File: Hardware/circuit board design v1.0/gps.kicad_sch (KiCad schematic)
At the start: 1 part

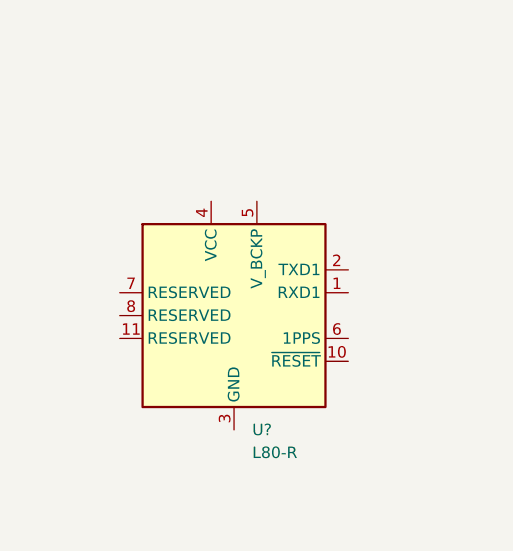
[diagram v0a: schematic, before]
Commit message: BMI088 schematic
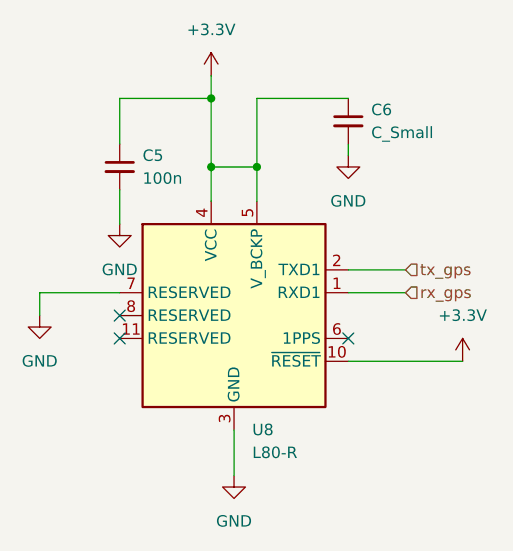
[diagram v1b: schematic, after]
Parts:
- added C5: 100n, symbol Device:C_Small
- added C6: C_Small, symbol Device:C_Small
- gave numbers to parts that had none: 1
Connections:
- net rx_gps: now reaches U8.1 (RXD1)
- net +3.3V: now reaches U8.10 (~{RESET})
- net +3.3V: now also U8.4 (VCC), U8.5 (V_BCKP), C5.1, C6.1
- net GND: now reaches U8.12 (GND), U8.3 (GND)
- net GND: now also U8.7 (RESERVED), C5.2, C6.2
- net tx_gps: now reaches U8.2 (TXD1)
- no-connect marks 0 -> 3
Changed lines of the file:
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@@
 (kicad_sch (version 20211123) (generator eeschema)
   (paper "A4")
+  (junction (at 124.46 60.96) (diameter 0) (color 0 0 0 0)
+  )
+  (junction (at 129.54 60.96) (diameter 0) (color 0 0 0 0)
+  )
+  (junction (at 124.46 53.34) (diameter 0) (color 0 0 0 0)
+  )
+  (no_connect (at 114.3 80.01))
+  (no_connect (at 139.7 80.01))
+  (no_connect (at 114.3 77.47))
+  (wire (pts (xy 114.3 53.34) (xy 124.46 53.34))
+    (stroke (width 0) (type default) (color 0 0 0 0))
+  )
+  (wire (pts (xy 114.3 63.5) (xy 114.3 67.31))
+    (stroke (width 0) (type default) (color 0 0 0 0))
+  )
+  (wire (pts (xy 114.3 74.93) (xy 105.41 74.93))
+    (stroke (width 0) (type default) (color 0 0 0 0))
+  )
+  (wire (pts (xy 139.7 53.34) (xy 129.54 53.34))
+    (stroke (width 0) (type default) (color 0 0 0 0))
+  )
+  (wire (pts (xy 124.46 53.34) (xy 124.46 60.96))
+    (stroke (width 0) (type default) (color 0 0 0 0))
+  )
+  (wire (pts (xy 127 90.17) (xy 127 95.25))
+    (stroke (width 0) (type default) (color 0 0 0 0))
+  )
+  (wire (pts (xy 129.54 53.34) (xy 129.54 60.96))
+    (stroke (width 0) (type default) (color 0 0 0 0))
+  )
+  (wire (pts (xy 139.7 72.39) (xy 146.05 72.39))
+    (stroke (width 0) (type default) (color 0 0 0 0))
+  )
+  (wire (pts (xy 124.46 60.96) (xy 124.46 64.77))
+    (stroke (width 0) (type default) (color 0 0 0 0))
+  )
+  (wire (pts (xy 139.7 74.93) (xy 146.05 74.93))
+    (stroke (width 0) (type default) (color 0 0 0 0))
+  )
+  (wire (pts (xy 124.46 60.96) (xy 129.54 60.96))
+    (stroke (width 0) (type default) (color 0 0 0 0))
+  )
+  (wire (pts (xy 139.7 82.55) (xy 152.4 82.55))
+    (stroke (width 0) (type default) (color 0 0 0 0))
+  )
+  (wire (pts (xy 105.41 74.93) (xy 105.41 77.47))
+    (stroke (width 0) (type default) (color 0 0 0 0))
+  )
+  (wire (pts (xy 129.54 60.96) (xy 129.54 64.77))
+    (stroke (width 0) (type default) (color 0 0 0 0))
+  )
+  (wire (pts (xy 124.46 50.8) (xy 124.46 53.34))
+    (stroke (width 0) (type default) (color 0 0 0 0))
+  )
+  (wire (pts (xy 139.7 58.42) (xy 139.7 59.69))
+    (stroke (width 0) (type default) (color 0 0 0 0))
+  )
+  (wire (pts (xy 114.3 58.42) (xy 114.3 53.34))
+    (stroke (width 0) (type default) (color 0 0 0 0))
+  )
+  (hierarchical_label "rx_gps" (shape input) (at 146.05 74.93 0)
+    (effects (font (size 1.27 1.27)) (justify left))
+  )
+  (hierarchical_label "tx_gps" (shape input) (at 146.05 72.39 0)
+    (effects (font (size 1.27 1.27)) (justify left))
+  )
+  (symbol (lib_id "power:GND") (at 105.41 77.47 0) (unit 1)
+    (in_bom yes) (on_board yes) (fields_autoplaced)
+    (property "Reference" "#PWR0120" (id 0) (at 105.41 83.82 0)
+      (effects (font (size 1.27 1.27)) hide)
+    )
+    (property "Value" "GND" (id 1) (at 105.41 82.55 0))
+    (property "Footprint" "" (id 2) (at 105.41 77.47 0)
+      (effects (font (size 1.27 1.27)) hide)
+    )
+    (property "Datasheet" "" (id 3) (at 105.41 77.47 0)
+      (effects (font (size 1.27 1.27)) hide)
+    )
+    (pin "1")
+  )
+  (symbol (lib_id "power:+3.3V") (at 152.4 82.55 0) (unit 1)
+    (in_bom yes) (on_board yes) (fields_autoplaced)
+    (property "Reference" "#PWR0117" (id 0) (at 152.4 86.36 0)
+      (effects (font (size 1.27 1.27)) hide)
+    )
+    (property "Value" "+3.3V" (id 1) (at 152.4 77.47 0))
+    (property "Footprint" "" (id 2) (at 152.4 82.55 0)
+      (effects (font (size 1.27 1.27)) hide)
+    )
+    (property "Datasheet" "" (id 3) (at 152.4 82.55 0)
+      (effects (font (size 1.27 1.27)) hide)
+    )
+    (pin "1")
+  )
+  (symbol (lib_id "power:+3.3V") (at 124.46 50.8 0) (unit 1)
+    (in_bom yes) (on_board yes) (fields_autoplaced)
+    (property "Reference" "#PWR0121" (id 0) (at 124.46 54.61 0)
+      (effects (font (size 1.27 1.27)) hide)
+    )
+    (property "Value" "+3.3V" (id 1) (at 124.46 45.72 0))
+    (property "Footprint" "" (id 2) (at 124.46 50.8 0)
+      (effects (font (size 1.27 1.27)) hide)
+    )
+    (property "Datasheet" "" (id 3) (at 124.46 50.8 0)
+      (effects (font (size 1.27 1.27)) hide)
+    )
+    (pin "1")
+  )
+  (symbol (lib_id "power:GND") (at 114.3 67.31 0) (unit 1)
+    (in_bom yes) (on_board yes) (fields_autoplaced)
+    (property "Reference" "#PWR0119" (id 0) (at 114.3 73.66 0)
+      (effects (font (size 1.27 1.27)) hide)
+    )
+    (property "Value" "GND" (id 1) (at 114.3 72.39 0))
+    (property "Footprint" "" (id 2) (at 114.3 67.31 0)
+      (effects (font (size 1.27 1.27)) hide)
+    )
+    (property "Datasheet" "" (id 3) (at 114.3 67.31 0)
+      (effects (font (size 1.27 1.27)) hide)
+    )
+    (pin "1")
+  )
+  (symbol (lib_id "power:GND") (at 127 95.25 0) (unit 1)
+    (in_bom yes) (on_board yes) (fields_autoplaced)
+    (property "Reference" "#PWR0118" (id 0) (at 127 101.6 0)
+      (effects (font (size 1.27 1.27)) hide)
+    )
+    (property "Value" "GND" (id 1) (at 127 100.33 0))
+    (property "Footprint" "" (id 2) (at 127 95.25 0)
+      (effects (font (size 1.27 1.27)) hide)
+    )
+    (property "Datasheet" "" (id 3) (at 127 95.25 0)
+      (effects (font (size 1.27 1.27)) hide)
+    )
+    (pin "1")
+  )
+  (symbol (lib_id "power:GND") (at 139.7 59.69 0) (unit 1)
+    (in_bom yes) (on_board yes) (fields_autoplaced)
+    (property "Reference" "#PWR0116" (id 0) (at 139.7 66.04 0)
+      (effects (font (size 1.27 1.27)) hide)
+    )
+    (property "Value" "GND" (id 1) (at 139.7 64.77 0))
+    (property "Footprint" "" (id 2) (at 139.7 59.69 0)
+      (effects (font (size 1.27 1.27)) hide)
+    )
+    (property "Datasheet" "" (id 3) (at 139.7 59.69 0)
+      (effects (font (size 1.27 1.27)) hide)
+    )
+    (pin "1")
+  )
   (symbol (lib_id "RF_GPS:L80-R") (at 127 77.47 0) (unit 1)
     (in_bom yes) (on_board yes) (fields_autoplaced)
-    (property "Reference" "U?" (id 0) (at 129.0194 90.17 0)
+    (property "Reference" "U8" (id 0) (at 129.0194 90.17 0)
       (effects (font (size 1.27 1.27)) (justify left))
     )
@@
     (pin "9")
   )
+  (symbol (lib_id "Device:C_Small") (at 139.7 55.88 0) (unit 1)
+    (in_bom yes) (on_board yes) (fields_autoplaced)
+    (property "Reference" "C6" (id 0) (at 142.24 54.6162 0)
+      (effects (font (size 1.27 1.27)) (justify left))
+    )
+    (property "Value" "C_Small" (id 1) (at 142.24 57.1562 0)
+      (effects (font (size 1.27 1.27)) (justify left))
+    )
+    (property "Footprint" "" (id 2) (at 139.7 55.88 0)
+      (effects (font (size 1.27 1.27)) hide)
+    )
+    (property "Datasheet" "~" (id 3) (at 139.7 55.88 0)
+      (effects (font (size 1.27 1.27)) hide)
+    )
+    (pin "1")
+    (pin "2")
+  )
+  (symbol (lib_id "Device:C_Small") (at 114.3 60.96 0) (unit 1)
+    (in_bom yes) (on_board yes) (fields_autoplaced)
+    (property "Reference" "C5" (id 0) (at 116.84 59.6962 0)
+      (effects (font (size 1.27 1.27)) (justify left))
+    )
+    (property "Value" "100n" (id 1) (at 116.84 62.2362 0)
+      (effects (font (size 1.27 1.27)) (justify left))
+    )
+    (property "Footprint" "" (id 2) (at 114.3 60.96 0)
+      (effects (font (size 1.27 1.27)) hide)
+    )
+    (property "Datasheet" "~" (id 3) (at 114.3 60.96 0)
+      (effects (font (size 1.27 1.27)) hide)
+    )
+    (pin "1")
+    (pin "2")
+  )
 )

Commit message: Created stm32mx project and started on layout
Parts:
- C5, C6: footprint (none) -> Capacitor_SMD:C_0603_1608Metric
- U8: footprint RF_GPS:Quectel_L80-R -> Components:Quectel_L80-R
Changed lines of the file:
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@@
     (effects (font (size 1.27 1.27)) (justify left))
   )
-  (hierarchical_label "tx_gps" (shape input) (at 146.05 72.39 0)
+  (hierarchical_label "tx_gps" (shape output) (at 146.05 72.39 0)
     (effects (font (size 1.27 1.27)) (justify left))
   )
@@
       (effects (font (size 1.27 1.27)) (justify left))
     )
-    (property "Footprint" "RF_GPS:Quectel_L80-R" (id 2) (at 127 100.33 0)
+    (property "Footprint" "Components:Quectel_L80-R" (id 2) (at 127 100.33 0)
       (effects (font (size 1.27 1.27)) hide)
     )
@@
       (effects (font (size 1.27 1.27)) (justify left))
     )
-    (property "Footprint" "" (id 2) (at 139.7 55.88 0)
+    (property "Footprint" "Capacitor_SMD:C_0603_1608Metric" (id 2) (at 139.7 55.88 0)
       (effects (font (size 1.27 1.27)) hide)
     )
@@
       (effects (font (size 1.27 1.27)) (justify left))
     )
-    (property "Footprint" "" (id 2) (at 114.3 60.96 0)
+    (property "Footprint" "Capacitor_SMD:C_0603_1608Metric" (id 2) (at 114.3 60.96 0)
       (effects (font (size 1.27 1.27)) hide)
     )

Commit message: Added extra cap in case its needed
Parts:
- C5: value 100n -> 100nF
- C6: value C_Small -> 100nF
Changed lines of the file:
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@@
       (effects (font (size 1.27 1.27)) (justify left))
     )
-    (property "Value" "C_Small" (id 1) (at 142.24 57.1562 0)
+    (property "Value" "100nF" (id 1) (at 142.24 57.1562 0)
       (effects (font (size 1.27 1.27)) (justify left))
     )
@@
       (effects (font (size 1.27 1.27)) (justify left))
     )
-    (property "Value" "100n" (id 1) (at 116.84 62.2362 0)
+    (property "Value" "100nF" (id 1) (at 116.84 62.2362 0)
       (effects (font (size 1.27 1.27)) (justify left))
     )

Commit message: Redid footprint for buzzer
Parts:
- U8: value L80-R -> L80-M39
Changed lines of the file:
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@@
       (effects (font (size 1.27 1.27)) (justify left))
     )
-    (property "Value" "L80-R" (id 1) (at 129.0194 92.71 0)
+    (property "Value" "L80-M39" (id 1) (at 129.0194 92.71 0)
       (effects (font (size 1.27 1.27)) (justify left))
     )
